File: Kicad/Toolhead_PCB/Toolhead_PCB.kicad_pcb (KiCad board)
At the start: 2 copper layers, 49.8 x 28 mm, 10 parts, among them J1 Conn_02x07_Top_Bottom, J2 Motor, J3 Hotend Fan, J4 Part Cooling Fan, J5 Heater, J6 Thermistor, J7 X-Endstop, J8 Part Cooling Fan

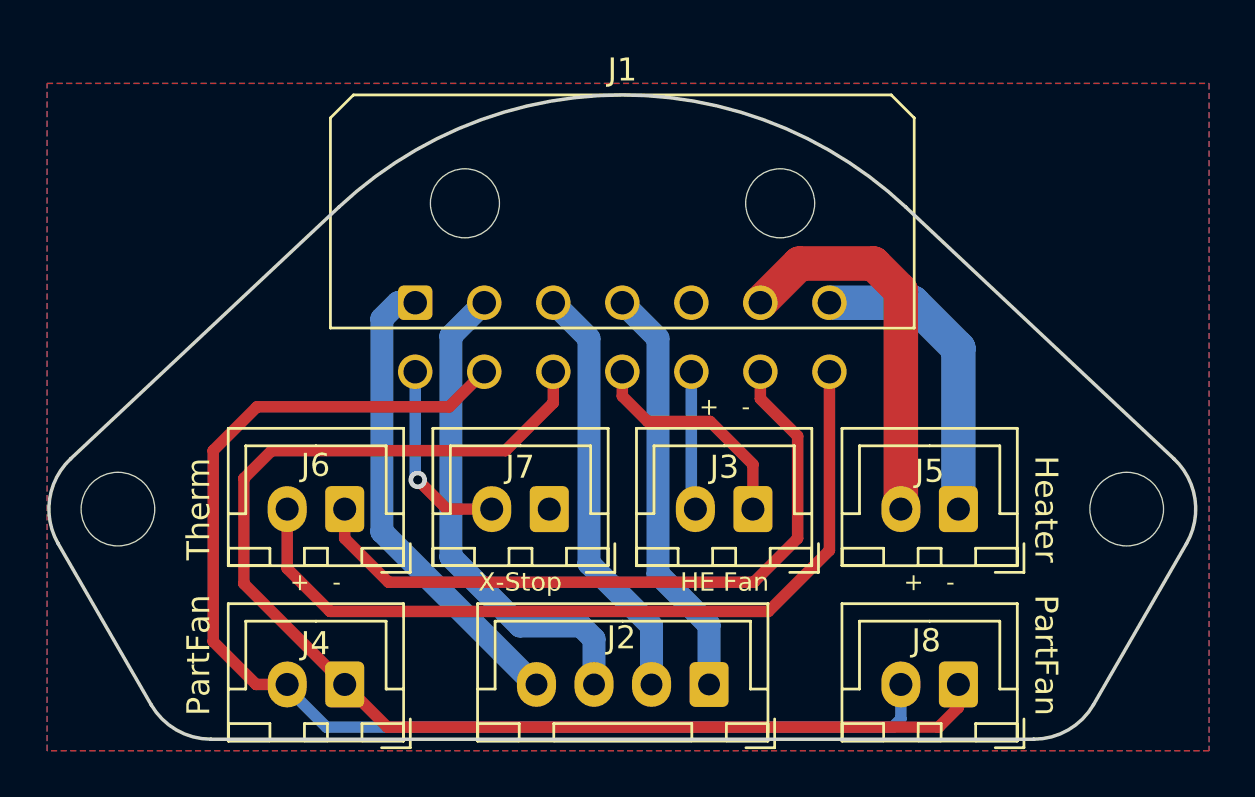
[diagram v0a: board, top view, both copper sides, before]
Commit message: Added accelerometer to Toolhead PCB, modified connector to 20-pin Molex Micro Fit
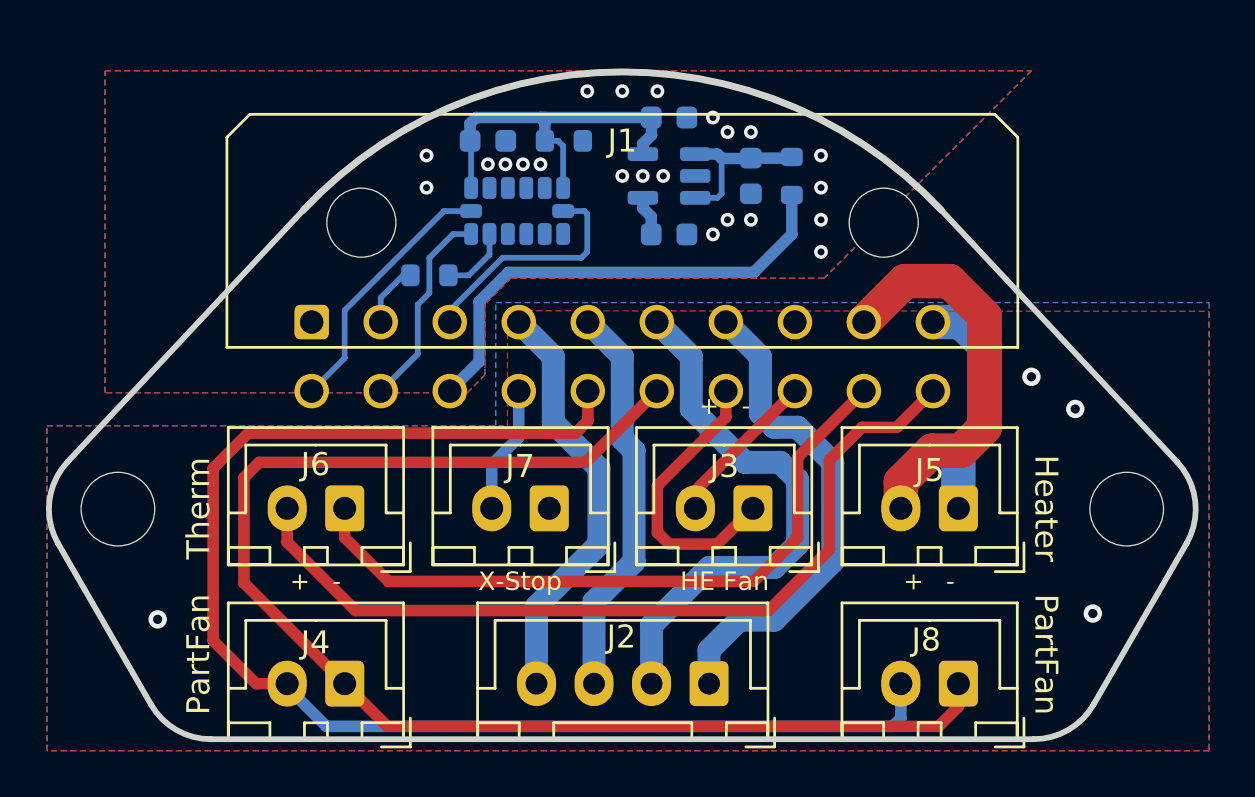
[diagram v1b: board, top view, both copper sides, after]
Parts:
- added C1: 4.7u/16V/X5R, Capacitor_SMD:C_0603_1608Metric, B.Cu at (105.6, 85.5)
- added C2: 10n/NP0, Capacitor_SMD:C_0603_1608Metric, B.Cu at (102.0, 88.1)
- added C3: 4.7u/16V/X5R, Capacitor_SMD:C_0603_1608Metric, B.Cu at (102.0, 83.0)
- added C4: 10n/NP0, Capacitor_SMD:C_0603_1608Metric, B.Cu at (94.2, 84.0)
- added R1: 10R, Resistor_SMD:R_0603_1608Metric, B.Cu at (107.4, 85.5)
- added R2: 10K, Resistor_SMD:R_0603_1608Metric, B.Cu at (97.5, 84.0)
- added R3: 10R, Resistor_SMD:R_0603_1608Metric, B.Cu at (91.6, 89.8)
- added U1: ADXL343, Package_LGA:LGA-14_3x5mm_P0.8mm_LayoutBorder1x6y, B.Cu at (95.4, 87.0)
- added U2: LP2985-3.3, Package_TO_SOT_SMD:SOT-23-5, B.Cu at (102.0, 85.5)
- J1: value Conn_02x07_Top_Bottom -> Conn_02x10_Top_Bottom; footprint Toolhead_PCB:Molex_Micro-Fit_3.0_43045-1400_2x07_P3.00mm_Horizontal -> Toolhead_PCB:Molex_Micro-Fit_3.0_43045-2000_2x10_P3.00mm_Horizontal
- moved J1 4.58 mm to (86.5, 91.9)
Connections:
- J1 pad 1: /Motor_A1 -> GND1
- J1 pad 10: /PartFan- -> /Heater1
- J1 pad 11: /Hotend_Fan- -> /ADXL_SCLK
- J1 pad 12: /Hotend_Fan+ -> /ADXL_SDI
- J1 pad 13: /Thermistor_1 -> VCC
- J1 pad 14: /Thermistor_2 -> /Endstop_Sig
- J1 pad 2: /Motor_A2 -> /ADXL_SDO
- J1 pad 3: /Motor_B1 -> /ADXL_CS
- J1 pad 4: /Motor_B2 -> /Motor_A1
- J1 pad 5: GND -> /Motor_A2
- J1 pad 6: /Heater2 -> /Motor_B1
- J1 pad 7: /Heater1 -> /Motor_B2
- J1 pad 8: /Endstop_Sig -> GND
- J1 pad 9: /PartFan+ -> /Heater2
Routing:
- net VCC: track 0.00 -> 20.9 mm
- net +3V3: track 0.00 -> 16.6 mm
- net /ADXL_SCLK: track 0.00 -> 11.4 mm
- net /ADXL_CS: track 0.00 -> 10.3 mm
- net /ADXL_SDI: track 0.00 -> 8.91 mm
- net Net-(C1-Pad1): track 0.00 -> 7.05 mm
- net /Motor_B1: track 18.4 -> 23.4 mm
- net /PartFan+: track 54.7 -> 59.1 mm
- net /Motor_A2: track 21.3 -> 17.3 mm
- net /PartFan-: track 55.7 -> 59.1 mm
- net /Heater1: track 13.4 -> 10.2 mm
- net Net-(R3-Pad2): track 0.00 -> 3.05 mm
- net /Motor_B2: track 18.2 -> 21.2 mm
- net /Endstop_Sig: track 8.49 -> 5.58 mm, vias 1 -> 0
- net /ADXL_SDO: track 0.00 -> 2.75 mm
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- added copper zone on B.Cu, net GND1
- added copper zone on F.Cu, net GND1
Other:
- board size 49.8 x 28 mm -> 49.8 x 29 mm
- net class Default removed

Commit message: Minor changes, added new schematic and project file
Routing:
- net /ADXL_CS: track 10.3 -> 13.5 mm
- net /PartFan+: track 59.1 -> 57.2 mm
- net GND: vias 4 -> 8
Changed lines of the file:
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@@
     (property "Sheetname" "")
     (attr smd)
-    (fp_text reference "U1" (at -1.27 3.048 90) (layer "B.SilkS")
+    (fp_text reference "U1" (at -0.546 3.428 90) (layer "B.SilkS")
       (effects (font (size 1 1) (thickness 0.15)) (justify mirror))
     )
@@
     (effects (font (size 0.8 0.8) (thickness 0.15)))
   )
-  (via (at 120.447 104.538) (size 0.8) (drill 0.4) (layers "F.Cu" "B.Cu") (free) (net 1))
-  (via (at 117.78 94.251) (size 0.8) (drill 0.4) (layers "F.Cu" "B.Cu") (free) (net 1))
-  (via (at 79.807 104.792) (size 0.8) (drill 0.4) (layers "F.Cu" "B.Cu") (free) (net 1))
-  (via (at 119.685 95.648) (size 0.8) (drill 0.4) (layers "F.Cu" "B.Cu") (free) (net 1))
+  (via (at 93 107.5) (size 0.6) (drill 0.3) (layers "F.Cu" "B.Cu") (free) (net 1))
+  (via (at 107 107.5) (size 0.6) (drill 0.3) (layers "F.Cu" "B.Cu") (free) (net 1))
+  (via (at 90.985974 107.496687) (size 0.6) (drill 0.3) (layers "F.Cu" "B.Cu") (free) (net 1))
+  (via (at 120.447 104.538) (size 0.6) (drill 0.3) (layers "F.Cu" "B.Cu") (free) (net 1))
+  (via (at 109 107.5) (size 0.6) (drill 0.3) (layers "F.Cu" "B.Cu") (free) (net 1))
+  (via (at 117.78 94.251) (size 0.6) (drill 0.3) (layers "F.Cu" "B.Cu") (free) (net 1))
+  (via (at 79.807 104.792) (size 0.6) (drill 0.3) (layers "F.Cu" "B.Cu") (free) (net 1))
+  (via (at 119.685 95.648) (size 0.6) (drill 0.3) (layers "F.Cu" "B.Cu") (free) (net 1))
   (segment (start 103.175 99.966) (end 103.175 99.197) (width 0.5) (layer "F.Cu") (net 2))
   (segment (start 103.175 99.197) (end 107.5 94.872) (width 0.5) (layer "F.Cu") (net 2))
@@
   (segment (start 104.5 96.008) (end 104.5 94.872) (width 0.5) (layer "F.Cu") (net 3))
   (segment (start 102.032 101.524) (end 104.117 101.524) (width 0.5) (layer "F.Cu") (net 3))
+  (segment (start 113.94052 109.25048) (end 114.605 108.586) (width 0.5) (layer "F.Cu") (net 4))
   (segment (start 83.55501 98.63099) (end 84.218 97.968) (width 0.5) (layer "F.Cu") (net 4))
   (segment (start 84.218 97.968) (end 98.404 97.968) (width 0.5) (layer "F.Cu") (net 4))
-  (segment (start 87.935 107.586) (end 89.78999 109.44099) (width 0.5) (layer "F.Cu") (net 4))
-  (segment (start 113.75001 109.44099) (end 114.605 108.586) (width 0.5) (layer "F.Cu") (net 4))
+  (segment (start 87.935 107.586) (end 89.59948 109.25048) (width 0.5) (layer "F.Cu") (net 4))
   (segment (start 114.605 108.586) (end 114.605 107.586) (width 0.5) (layer "F.Cu") (net 4))
   (segment (start 87.935 107.586) (end 83.55501 103.20601) (width 0.5) (layer "F.Cu") (net 4))
   (segment (start 83.55501 103.20601) (end 83.55501 98.63099) (width 0.5) (layer "F.Cu") (net 4))
+  (segment (start 89.59948 109.25048) (end 113.94052 109.25048) (width 0.5) (layer "F.Cu") (net 4))
   (segment (start 98.404 97.968) (end 101.5 94.872) (width 0.5) (layer "F.Cu") (net 4))
-  (segment (start 89.78999 109.44099) (end 113.75001 109.44099) (width 0.5) (layer "F.Cu") (net 4))
+  (segment (start 83.744 96.698) (end 97.968 96.698) (width 0.5) (layer "F.Cu") (net 5))
   (segment (start 82.22 98.222) (end 83.744 96.698) (width 0.5) (layer "F.Cu") (net 5))
-  (segment (start 84.085 107.586) (end 82.22 105.721) (width 0.5) (layer "F.Cu") (net 5))
-  (segment (start 82.22 105.721) (end 82.22 98.222) (width 0.5) (layer "F.Cu") (net 5))
-  (segment (start 85.435 107.586) (end 84.085 107.586) (width 0.5) (layer "F.Cu") (net 5))
-  (segment (start 83.744 96.698) (end 97.968 96.698) (width 0.5) (layer "F.Cu") (net 5))
+  (segment (start 97.968 96.698) (end 98.5 96.166) (width 0.5) (layer "F.Cu") (net 5))
+  (segment (start 85.435 106.7964) (end 82.22 103.5814) (width 0.5) (layer "F.Cu") (net 5))
+  (segment (start 85.435 107.586) (end 85.435 106.7964) (width 0.5) (layer "F.Cu") (net 5))
+  (segment (start 82.22 103.5814) (end 82.22 98.222) (width 0.5) (layer "F.Cu") (net 5))
   (segment (start 98.5 96.166) (end 98.5 94.872) (width 0.5) (layer "F.Cu") (net 5))
-  (segment (start 97.968 96.698) (end 98.5 96.166) (width 0.5) (layer "F.Cu") (net 5))
-  (segment (start 87.13999 109.44099) (end 111.75001 109.44099) (width 0.5) (layer "B.Cu") (net 5))
-  (segment (start 112.105 109.086) (end 112.105 107.586) (width 0.5) (layer "B.Cu") (net 5))
-  (segment (start 85.435 107.586) (end 85.435 107.736) (width 0.5) (layer "B.Cu") (net 5))
-  (segment (start 111.75001 109.44099) (end 112.105 109.086) (width 0.5) (layer "B.Cu") (net 5))
-  (segment (start 85.435 107.736) (end 87.13999 109.44099) (width 0.5) (layer "B.Cu") (net 5))
+  (segment (start 87.09948 109.25048) (end 110.44052 109.25048) (width 0.5) (layer "B.Cu") (net 5))
+  (segment (start 110.44052 109.25048) (end 112.105 107.586) (width 0.5) (layer "B.Cu") (net 5))
+  (segment (start 85.435 107.586) (end 87.09948 109.25048) (width 0.5) (layer "B.Cu") (net 5))
   (segment (start 85.435 99.966) (end 85.435 101.437) (width 0.5) (layer "F.Cu") (net 6))
   (segment (start 111.928 96.444) (end 113.5 94.872) (width 0.5) (layer "F.Cu") (net 6))
@@
   (segment (start 114.605 97.587) (end 115.748 96.444) (width 1.5) (layer "B.Cu") (net 9))
   (segment (start 115.748 96.444) (end 115.748 92.888) (width 1.5) (layer "B.Cu") (net 9))
-  (segment (start 114.224 90.094) (end 112.278 90.094) (width 1.5) (layer "F.Cu") (net 10))
-  (segment (start 115.748 96.444) (end 115.748 91.618) (width 1.5) (layer "F.Cu") (net 10))
+  (segment (start 114.732 97.46) (end 115.748 96.444) (width 1.5) (layer "F.Cu") (net 10))
   (segment (start 112.105 98.817) (end 113.462 97.46) (width 1.5) (layer "F.Cu") (net 10))
+  (segment (start 112.105 99.966) (end 112.105 98.817) (width 1.5) (layer "F.Cu") (net 10))
+  (segment (start 115.748 96.444) (end 115.748 91.364) (width 1.5) (layer "F.Cu") (net 10))
   (segment (start 113.462 97.46) (end 114.732 97.46) (width 1.5) (layer "F.Cu") (net 10))
-  (segment (start 112.105 99.966) (end 112.105 98.817) (width 1.5) (layer "F.Cu") (net 10))
-  (segment (start 114.732 97.46) (end 115.748 96.444) (width 1.5) (layer "F.Cu") (net 10))
-  (segment (start 115.748 91.618) (end 114.224 90.094) (width 1.5) (layer "F.Cu") (net 10))
-  (segment (start 112.278 90.094) (end 110.5 91.872) (width 1.5) (layer "F.Cu") (net 10))
+  (segment (start 115.748 91.364) (end 114.384 90) (width 1.5) (layer "F.Cu") (net 10))
+  (segment (start 114.384 90) (end 112.372 90) (width 1.5) (layer "F.Cu") (net 10))
+  (segment (start 112.372 90) (end 110.5 91.872) (width 1.5) (layer "F.Cu") (net 10))
   (segment (start 105.08 104.826) (end 106.604 104.826) (width 1) (layer "B.Cu") (net 11))
   (segment (start 106.000489 93.372489) (end 106.000489 95.840489) (width 1) (layer "B.Cu") (net 11))
@@
   (via (at 95.682 85.014) (size 0.6) (drill 0.3) (layers "F.Cu" "B.Cu") (free) (net 21))
   (via (at 101.524 81.839) (size 0.6) (drill 0.3) (layers "F.Cu" "B.Cu") (free) (net 21))
-  (via (at 108.636 86.03) (size 0.6) (drill 0.3) (layers "F.Cu" "B.Cu") (free) (net 21))
+  (via (at 109.5 85.5) (size 0.6) (drill 0.3) (layers "F.Cu" "B.Cu") (free) (net 21))
   (via (at 96.444 85.014) (size 0.6) (drill 0.3) (layers "F.Cu" "B.Cu") (free) (net 21))
   (via (at 100.889 85.522) (size 0.6) (drill 0.3) (layers "F.Cu" "B.Cu") (free) (net 21))
@@
   (via (at 108.636 88.824) (size 0.6) (drill 0.3) (layers "F.Cu" "B.Cu") (free) (net 21))
   (via (at 100 81.839) (size 0.6) (drill 0.3) (layers "F.Cu" "B.Cu") (free) (net 21))
-  (via (at 91.491 86.03) (size 0.6) (drill 0.3) (layers "F.Cu" "B.Cu") (free) (net 21))
+  (via (at 90.5 85.5) (size 0.6) (drill 0.3) (layers "F.Cu" "B.Cu") (free) (net 21))
   (via (at 103.937 88.062) (size 0.6) (drill 0.3) (layers "F.Cu" "B.Cu") (free) (net 21))
   (via (at 104.572 87.427) (size 0.6) (drill 0.3) (layers "F.Cu" "B.Cu") (free) (net 21))
@@
   (segment (start 98.222 89.078) (end 94.793 89.078) (width 0.25) (layer "B.Cu") (net 27))
   (segment (start 98.476 87.173) (end 98.476 88.824) (width 0.25) (layer "B.Cu") (net 27))
+  (segment (start 98.285 83.998) (end 98.285 84.823) (width 0.25) (layer "B.Cu") (net 27))
+  (segment (start 98.476 85.014) (end 98.476 86.919) (width 0.25) (layer "B.Cu") (net 27))
+  (segment (start 98.476 86.919) (end 98.349 87.046) (width 0.25) (layer "B.Cu") (net 27))
+  (segment (start 98.285 84.823) (end 98.476 85.014) (width 0.25) (layer "B.Cu") (net 27))
   (segment (start 92.5 91.371) (end 92.5 91.872) (width 0.25) (layer "B.Cu") (net 27))
   (segment (start 87.935 91.364) (end 87.935 93.437) (width 0.25) (layer "B.Cu") (net 28))

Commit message: Updated part number of ICs
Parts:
- U1: value ADXL343 -> ADXL345BCCZ
- U2: value LP2985-3.3 -> LP2985-33DBVR
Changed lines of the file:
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@@
     (pad "" np_thru_hole circle (at 2.16 -4.32) (size 3 3) (drill 3) (layers *.Cu *.Mask))
     (pad "" np_thru_hole circle (at 24.86 -4.32) (size 3 3) (drill 3) (layers *.Cu *.Mask))
-    (pad "1" thru_hole roundrect (at 0 0) (size 1.5 1.5) (drill 1.02) (layers *.Cu *.Mask) (roundrect_rratio 0.166667)
+    (pad "1" thru_hole roundrect (at 0 0) (size 1.5 1.5) (drill 1.02) (layers *.Cu *.Mask) (roundrect_rratio 0.1666673333)
       (net 21 "GND1") (pinfunction "Pin_1") (pintype "passive"))
     (pad "2" thru_hole circle (at 3 0) (size 1.5 1.5) (drill 1.02) (layers *.Cu *.Mask)
@@
     (fp_line (start 4.95 3.4) (end 4.95 -2.35) (layer "F.Fab") (width 0.1))
     (fp_line (start 4.95 -2.35) (end -2.45 -2.35) (layer "F.Fab") (width 0.1))
-    (pad "1" thru_hole roundrect locked (at 0 0 180) (size 1.7 2) (drill 1) (layers *.Cu *.Mask) (roundrect_rratio 0.147059)
+    (pad "1" thru_hole roundrect locked (at 0 0 180) (size 1.7 2) (drill 1) (layers *.Cu *.Mask) (roundrect_rratio 0.1470588235)
       (net 1 "GND") (pinfunction "Pin_1") (pintype "passive"))
     (pad "2" thru_hole oval locked (at 2.5 0 180) (size 1.7 2) (drill 1) (layers *.Cu *.Mask)
@@
     (fp_line (start -2.45 3.4) (end 4.95 3.4) (layer "F.Fab") (width 0.1))
     (fp_line (start -0.625 -2.35) (end 0 -1.35) (layer "F.Fab") (width 0.1))
-    (pad "1" thru_hole roundrect locked (at 0 0 180) (size 1.7 2) (drill 1) (layers *.Cu *.Mask) (roundrect_rratio 0.147059)
+    (pad "1" thru_hole roundrect locked (at 0 0 180) (size 1.7 2) (drill 1) (layers *.Cu *.Mask) (roundrect_rratio 0.1470588235)
       (net 9 "/Heater1") (pinfunction "Pin_1") (pintype "passive"))
     (pad "2" thru_hole oval locked (at 2.5 0 180) (size 1.7 2) (drill 1) (layers *.Cu *.Mask)
@@
     (fp_line (start 4.95 3.4) (end 4.95 -2.35) (layer "F.Fab") (width 0.1))
     (fp_line (start -2.45 3.4) (end 4.95 3.4) (layer "F.Fab") (width 0.1))
-    (pad "1" thru_hole roundrect locked (at 0 0 180) (size 1.7 2) (drill 1) (layers *.Cu *.Mask) (roundrect_rratio 0.147059)
+    (pad "1" thru_hole roundrect locked (at 0 0 180) (size 1.7 2) (drill 1) (layers *.Cu *.Mask) (roundrect_rratio 0.1470588235)
       (net 3 "/Hotend_Fan-") (pinfunction "Pin_1") (pintype "passive"))
     (pad "2" thru_hole oval locked (at 2.5 0 180) (size 1.7 2) (drill 1) (layers *.Cu *.Mask)
@@
     (fp_line (start -2.45 3.4) (end 4.95 3.4) (layer "F.Fab") (width 0.1))
     (fp_line (start 4.95 -2.35) (end -2.45 -2.35) (layer "F.Fab") (width 0.1))
-    (pad "1" thru_hole roundrect locked (at 0 0 180) (size 1.7 2) (drill 1) (layers *.Cu *.Mask) (roundrect_rratio 0.147059)
+    (pad "1" thru_hole roundrect locked (at 0 0 180) (size 1.7 2) (drill 1) (layers *.Cu *.Mask) (roundrect_rratio 0.1470588235)
       (net 7 "/Thermistor_1") (pinfunction "Pin_1") (pintype "passive"))
     (pad "2" thru_hole oval locked (at 2.5 0 180) (size 1.7 2) (drill 1) (layers *.Cu *.Mask)
@@
     (fp_line (start -2.45 3.4) (end 4.95 3.4) (layer "F.Fab") (width 0.1))
     (fp_line (start 0 -1.35) (end 0.625 -2.35) (layer "F.Fab") (width 0.1))
-    (pad "1" thru_hole roundrect locked (at 0 0 180) (size 1.7 2) (drill 1) (layers *.Cu *.Mask) (roundrect_rratio 0.147059)
+    (pad "1" thru_hole roundrect locked (at 0 0 180) (size 1.7 2) (drill 1) (layers *.Cu *.Mask) (roundrect_rratio 0.1470588235)
       (net 4 "/PartFan-") (pinfunction "Pin_1") (pintype "passive"))
     (pad "2" thru_hole oval locked (at 2.5 0 180) (size 1.7 2) (drill 1) (layers *.Cu *.Mask)
@@
     (fp_line (start -0.625 -2.35) (end 0 -1.35) (layer "F.Fab") (width 0.1))
     (fp_line (start 0 -1.35) (end 0.625 -2.35) (layer "F.Fab") (width 0.1))
-    (pad "1" thru_hole roundrect locked (at 0 0 180) (size 1.7 1.95) (drill 0.95) (layers *.Cu *.Mask) (roundrect_rratio 0.147059)
+    (pad "1" thru_hole roundrect locked (at 0 0 180) (size 1.7 1.95) (drill 0.95) (layers *.Cu *.Mask) (roundrect_rratio 0.1470588235)
       (net 11 "/Motor_B2") (pinfunction "Pin_1") (pintype "passive"))
     (pad "2" thru_hole oval locked (at 2.5 0 180) (size 1.7 1.95) (drill 0.95) (layers *.Cu *.Mask)
@@
     (fp_line (start -0.625 -2.35) (end 0 -1.35) (layer "F.Fab") (width 0.1))
     (fp_line (start 0 -1.35) (end 0.625 -2.35) (layer "F.Fab") (width 0.1))
-    (pad "1" thru_hole roundrect locked (at 0 0 180) (size 1.7 2) (drill 1) (layers *.Cu *.Mask) (roundrect_rratio 0.147059)
+    (pad "1" thru_hole roundrect locked (at 0 0 180) (size 1.7 2) (drill 1) (layers *.Cu *.Mask) (roundrect_rratio 0.1470588235)
       (net 4 "/PartFan-") (pinfunction "Pin_1") (pintype "passive"))
     (pad "2" thru_hole oval locked (at 2.5 0 180) (size 1.7 2) (drill 1) (layers *.Cu *.Mask)
@@
       (effects (font (size 1 1) (thickness 0.15)) (justify mirror))
     )
-    (fp_text value "ADXL343" (at 0 -3.45 90) (layer "B.Fab")
+    (fp_text value "ADXL345BCCZ" (at 0 -3.45 90) (layer "B.Fab")
       (effects (font (size 1 1) (thickness 0.15)) (justify mirror))
     )
@@
       (effects (font (size 1 1) (thickness 0.15)) (justify mirror))
     )
-    (fp_text value "LP2985-3.3" (at 0 -2.4) (layer "B.Fab")
-      (effects (font (size 1 1) (thickness 0.15)) (justify mirror))
-    )
+    (fp_text value "LP2985-33DBVR" (at 0 -2.4) (layer "B.Fab")
+      (effects (font (size 1 1) (thickness 0.15)) (justify mirror))
+    )
